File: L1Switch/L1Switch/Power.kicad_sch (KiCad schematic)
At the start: 60 parts, among them J3 Barrel_Jack, U3 TPS548A20RVE, U4 TPS565208, U5 TPS565208, U6 TPS565208

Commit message: Add some part info. Fix footprint size for 2kV caps. Add a plane cutout around the magnetics.
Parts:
- added M1, M2: Fan, Connector:FanPinHeader_1x03_P2.54mm_Vertical, symbol Motor:Fan_3pin
- C29, C30, C31: value 22 uF, 3.637 mΩ -> 22 uF, 3.637 mOhm; MFR Part# (none) -> GRM31CR61A226ME19L; Manufacturer (none) -> MuRata
- C32: value 2.2 nF, 1.268 Ω -> 2.2 nF, 1.268 Ohm; MFR Part# (none) -> CGA1A2X7R1E222K030BA; Manufacturer (none) -> TDK
- C33, C34: value 2.2 uF, 9.497 mΩ -> 2.2 uF, 9.497 mOhm; MFR Part# (none) -> GRM219R61E225KA12D; Manufacturer (none) -> MuRata
- C35: MFR Part# (none) -> C0805C104M5RACTU; Manufacturer (none) -> Kemet
- C36: value 470 pF, 5.548 Ω -> 470 pF, 5.548 Ohm; MFR Part# (none) -> CGA1A2X7R1H471K030BA; Manufacturer (none) -> TDK
- C37, C38, C39, C40, C41, C42: value 100 uF, 4.885 mΩ -> 100 uF, 4.885 mOhm; MFR Part# (none) -> GRM31CR60J107ME39L; Manufacturer (none) -> MuRata
- C43, C44, C50, C51, C57, C58: value 10 uF, 4.512 mΩ -> 10 uF, 4.512 mOhm; MFR Part# (none) -> GRM31CR61E106KA12L; Manufacturer (none) -> MuRata
- C45, C52, C59: value 100 nF, 1 mΩ -> 100 nF, 1 mOhm; MFR Part# (none) -> GRM155R71C104KA88D; Manufacturer (none) -> MuRata
- C46, C53, C60: MFR Part# (none) -> C0603C104Z3VACTU; Manufacturer (none) -> Kemet
- C47, C48, C49, C54, C55, C56, C61, C62, C63: value 22 uF, 1 mΩ -> 22 uF, 1 mOhm; MFR Part# (none) -> GRM188R60J226MEA0D; Manufacturer (none) -> MuRata
- D1: MFR Part# (none) -> P4SMA6.8CA; Manufacturer (none) -> Bourns
- F1: MFR Part# (none) -> 2920L700/12MR-A; Manufacturer (none) -> Littelfuse
- J3: MFR Part# (none) -> MJ-179PH; Manufacturer (none) -> Multicomp
- L1: value 1 uH, 3.5 mΩ -> 1 uH, 3.5 mOhm; MFR Part# (none) -> SRP1040-1R0M; Manufacturer (none) -> Bourns
- L2, L3, L4: value 2.2 uH, 13.2 mΩ -> 2.2 uH, 13.2 mOhm; MFR Part# (none) -> XAL5030-222MEB; Manufacturer (none) -> Coilcraft
- U3: MFR Part# (none) -> TPS548A20RVER; Manufacturer (none) -> Texas Instruments
- U4, U5, U6: MFR Part# (none) -> TPS565208DDCR; Manufacturer (none) -> Texas Instruments
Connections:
- net GND: now also M1.3 (-), M2.3 (-)
- net VIN_5V: now also M1.2 (+), M2.2 (+)
- no-connect marks 1 -> 3

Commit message: Update part numbers.
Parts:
- C32: MFR Part# CGA1A2X7R1E222K030BA -> CGA2B2X7R1H222K050BA
- C36: MFR Part# CGA1A2X7R1H471K030BA -> CGA2B2X7R1H471K050BA
- M1, M2: MFR Part# (none) -> 644874-3; Manufacturer (none) -> TE Connectivity
- R22: MFR Part# (none) -> RC0402FR-07249KL; Manufacturer (none) -> Yageo
- R23: MFR Part# (none) -> CRCW040244K2FKED; Manufacturer (none) -> Vishay
- R24: MFR Part# (none) -> RC0402FR-07105KL; Manufacturer (none) -> Yageo
- R25: MFR Part# (none) -> CRCW0402150KFKED; Manufacturer (none) -> Vishay
- R26: MFR Part# (none) -> RC0402FR-0768K1L; Manufacturer (none) -> Yageo
- R27: MFR Part# (none) -> CRCW04023R01FKED; Manufacturer (none) -> Vishay
- R28, R29, R31, R33, R35: value 10K -> 10K0; MFR Part# (none) -> CRCW040210K0FKED; Manufacturer (none) -> Vishay
- R30: MFR Part# (none) -> CRCW040233K2FKED; Manufacturer (none) -> Vishay
- R32: MFR Part# (none) -> CRCW040213K7FKED; Manufacturer (none) -> Vishay
- R34: MFR Part# (none) -> CRCW04023K09FKED; Manufacturer (none) -> Vishay
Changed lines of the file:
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@@
 (kicad_sch (version 20200608) (host eeschema "5.99.0-unknown-1973153~101~ubuntu20.04.1")
-  (page 12 12)
+  (page 1 12)
   (paper "B")
   (junction (at 26.67 80.01))
@@
   (junction (at 396.24 143.51))
   (junction (at 396.24 182.88))
-  (no_connect (at 340.36 93.98))
   (no_connect (at 345.44 55.88))
   (no_connect (at 356.87 93.98))
+  (no_connect (at 340.36 93.98))
   (wire (pts (xy 20.32 48.26) (xy 29.21 48.26))
     (stroke (width 0) (type solid) (color 0 0 0 0))
@@
       (effects (font (size 1.27 1.27)) hide)
     )
+    (property "MFR Part#" "RC0402FR-07249KL" (id 4) (at 88.9 92.71 0)
+      (effects (font (size 1.27 1.27)) hide)
+    )
+    (property "Manufacturer" "Yageo" (id 5) (at 88.9 92.71 0)
+      (effects (font (size 1.27 1.27)) hide)
+    )
   )
   (symbol (lib_id "Device:R_US") (at 88.9 102.87 0) (unit 1)
@@
       (effects (font (size 1.27 1.27)) hide)
     )
+    (property "MFR Part#" "CRCW040244K2FKED" (id 4) (at 88.9 102.87 0)
+      (effects (font (size 1.27 1.27)) hide)
+    )
+    (property "Manufacturer" "Vishay" (id 5) (at 88.9 102.87 0)
+      (effects (font (size 1.27 1.27)) hide)
+    )
   )
   (symbol (lib_id "Device:R_US") (at 92.71 81.28 90) (unit 1)
@@
       (effects (font (size 1.27 1.27)) hide)
     )
+    (property "MFR Part#" "RC0402FR-07105KL" (id 4) (at 92.71 81.28 0)
+      (effects (font (size 1.27 1.27)) hide)
+    )
+    (property "Manufacturer" "Yageo" (id 5) (at 92.71 81.28 0)
+      (effects (font (size 1.27 1.27)) hide)
+    )
   )
   (symbol (lib_id "Device:R_US") (at 99.06 77.47 0) (unit 1)
@@
       (effects (font (size 1.27 1.27)) hide)
     )
+    (property "MFR Part#" "CRCW0402150KFKED" (id 4) (at 99.06 77.47 0)
+      (effects (font (size 1.27 1.27)) hide)
+    )
+    (property "Manufacturer" "Vishay" (id 5) (at 99.06 77.47 0)
+      (effects (font (size 1.27 1.27)) hide)
+    )
   )
   (symbol (lib_id "Device:R_US") (at 162.56 156.21 0) (unit 1)
@@
       (effects (font (size 1.27 1.27)) hide)
     )
+    (property "MFR Part#" "CRCW040213K7FKED" (id 4) (at 162.56 156.21 0)
+      (effects (font (size 1.27 1.27)) hide)
+    )
+    (property "Manufacturer" "Vishay" (id 5) (at 162.56 156.21 0)
+      (effects (font (size 1.27 1.27)) hide)
+    )
   )
   (symbol (lib_id "Device:R_US") (at 162.56 175.26 0) (unit 1)
@@
       (effects (font (size 1.27 1.27)) (justify left))
     )
-    (property "Value" "10K" (id 1) (at 164.211 176.403 0)
+    (property "Value" "10K0" (id 1) (at 164.211 176.403 0)
       (effects (font (size 1.27 1.27)) (justify left))
     )
@@
       (effects (font (size 1.27 1.27)) hide)
     )
+    (property "MFR Part#" "CRCW040210K0FKED" (id 4) (at 162.56 175.26 0)
+      (effects (font (size 1.27 1.27)) hide)
+    )
+    (property "Manufacturer" "Vishay" (id 5) (at 162.56 175.26 0)
+      (effects (font (size 1.27 1.27)) hide)
+    )
   )
   (symbol (lib_id "Device:R_US") (at 162.56 226.06 0) (unit 1)
@@
       (effects (font (size 1.27 1.27)) hide)
     )
+    (property "MFR Part#" "CRCW040233K2FKED" (id 4) (at 162.56 226.06 0)
+      (effects (font (size 1.27 1.27)) hide)
+    )
+    (property "Manufacturer" "Vishay" (id 5) (at 162.56 226.06 0)
+      (effects (font (size 1.27 1.27)) hide)
+    )
   )
   (symbol (lib_id "Device:R_US") (at 162.56 245.11 0) (unit 1)
@@
       (effects (font (size 1.27 1.27)) (justify left))
     )
-    (property "Value" "10K" (id 1) (at 164.211 246.253 0)
+    (property "Value" "10K0" (id 1) (at 164.211 246.253 0)
       (effects (font (size 1.27 1.27)) (justify left))
     )
@@
       (effects (font (size 1.27 1.27)) hide)
     )
+    (property "MFR Part#" "CRCW040210K0FKED" (id 4) (at 162.56 245.11 0)
+      (effects (font (size 1.27 1.27)) hide)
+    )
+    (property "Manufacturer" "Vishay" (id 5) (at 162.56 245.11 0)
+      (effects (font (size 1.27 1.27)) hide)
+    )
   )
   (symbol (lib_id "Device:R_US") (at 167.64 85.09 0) (unit 1)
@@
       (effects (font (size 1.27 1.27)) hide)
     )
+    (property "MFR Part#" "RC0402FR-0768K1L" (id 4) (at 167.64 85.09 0)
+      (effects (font (size 1.27 1.27)) hide)
+    )
+    (property "Manufacturer" "Yageo" (id 5) (at 167.64 85.09 0)
+      (effects (font (size 1.27 1.27)) hide)
+    )
   )
   (symbol (lib_id "Device:R_US") (at 181.61 91.44 0) (unit 1)
@@
       (effects (font (size 1.27 1.27)) hide)
     )
+    (property "MFR Part#" "CRCW04023R01FKED" (id 4) (at 181.61 91.44 0)
+      (effects (font (size 1.27 1.27)) hide)
+    )
+    (property "Manufacturer" "Vishay" (id 5) (at 181.61 91.44 0)
+      (effects (font (size 1.27 1.27)) hide)
+    )
   )
   (symbol (lib_id "Device:R_US") (at 212.09 59.69 0) (unit 1)
@@
       (effects (font (size 1.27 1.27)) (justify left))
     )
-    (property "Value" "10K" (id 1) (at 213.741 60.833 0)
+    (property "Value" "10K0" (id 1) (at 213.741 60.833 0)
       (effects (font (size 1.27 1.27)) (justify left))
     )
@@
       (effects (font (size 1.27 1.27)) hide)
     )
+    (property "MFR Part#" "CRCW040210K0FKED" (id 4) (at 212.09 59.69 0)
+      (effects (font (size 1.27 1.27)) hide)
+    )
+    (property "Manufacturer" "Vishay" (id 5) (at 212.09 59.69 0)
+      (effects (font (size 1.27 1.27)) hide)
+    )
   )
   (symbol (lib_id "Device:R_US") (at 212.09 78.74 0) (unit 1)
@@
       (effects (font (size 1.27 1.27)) (justify left))
     )
-    (property "Value" "10K" (id 1) (at 213.741 79.883 0)
+    (property "Value" "10K0" (id 1) (at 213.741 79.883 0)
       (effects (font (size 1.27 1.27)) (justify left))
     )
@@
       (effects (font (size 1.27 1.27)) hide)
     )
+    (property "MFR Part#" "CRCW040210K0FKED" (id 4) (at 212.09 78.74 0)
+      (effects (font (size 1.27 1.27)) hide)
+    )
+    (property "Manufacturer" "Vishay" (id 5) (at 212.09 78.74 0)
+      (effects (font (size 1.27 1.27)) hide)
+    )
   )
   (symbol (lib_id "Device:R_US") (at 356.87 156.21 0) (unit 1)
@@
       (effects (font (size 1.27 1.27)) hide)
     )
+    (property "MFR Part#" "CRCW04023K09FKED" (id 4) (at 356.87 156.21 0)
+      (effects (font (size 1.27 1.27)) hide)
+    )
+    (property "Manufacturer" "Vishay" (id 5) (at 356.87 156.21 0)
+      (effects (font (size 1.27 1.27)) hide)
+    )
   )
   (symbol (lib_id "Device:R_US") (at 356.87 175.26 0) (unit 1)
@@
       (effects (font (size 1.27 1.27)) (justify left))
     )
-    (property "Value" "10K" (id 1) (at 358.521 176.403 0)
+    (property "Value" "10K0" (id 1) (at 358.521 176.403 0)
       (effects (font (size 1.27 1.27)) (justify left))
     )
@@
     )
     (property "Datasheet" "~" (id 3) (at 356.87 175.26 0)
+      (effects (font (size 1.27 1.27)) hide)
+    )
+    (property "MFR Part#" "CRCW040210K0FKED" (id 4) (at 356.87 175.26 0)
+      (effects (font (size 1.27 1.27)) hide)
+    )
+    (property "Manufacturer" "Vishay" (id 5) (at 356.87 175.26 0)
       (effects (font (size 1.27 1.27)) hide)
     )
@@
       (effects (font (size 1.27 1.27)) hide)
     )
-    (property "MFR Part#" "CGA1A2X7R1E222K030BA" (id 4) (at 69.85 63.5 0)
+    (property "MFR Part#" "CGA2B2X7R1H222K050BA" (id 4) (at 69.85 63.5 0)
       (effects (font (size 1.27 1.27)) hide)
     )
@@
       (effects (font (size 1.27 1.27)) hide)
     )
-    (property "MFR Part#" "CGA1A2X7R1H471K030BA" (id 4) (at 181.61 74.93 0)
+    (property "MFR Part#" "CGA2B2X7R1H471K050BA" (id 4) (at 181.61 74.93 0)
       (effects (font (size 1.27 1.27)) hide)
     )
@@
       (effects (font (size 1.27 1.27)) hide)
     )
+    (property "MFR Part#" "644874-3" (id 4) (at 347.98 93.98 0)
+      (effects (font (size 1.27 1.27)) hide)
+    )
+    (property "Manufacturer" "TE Connectivity" (id 5) (at 347.98 93.98 0)
+      (effects (font (size 1.27 1.27)) hide)
+    )
   )
   (symbol (lib_id "Motor:Fan_3pin") (at 364.49 93.98 0) (unit 1)
@@
       (effects (font (size 1.27 1.27)) hide)
     )
+    (property "MFR Part#" "644874-3" (id 4) (at 364.49 93.98 0)
+      (effects (font (size 1.27 1.27)) hide)
+    )
+    (property "Manufacturer" "TE Connectivity" (id 5) (at 364.49 93.98 0)
+      (effects (font (size 1.27 1.27)) hide)
+    )

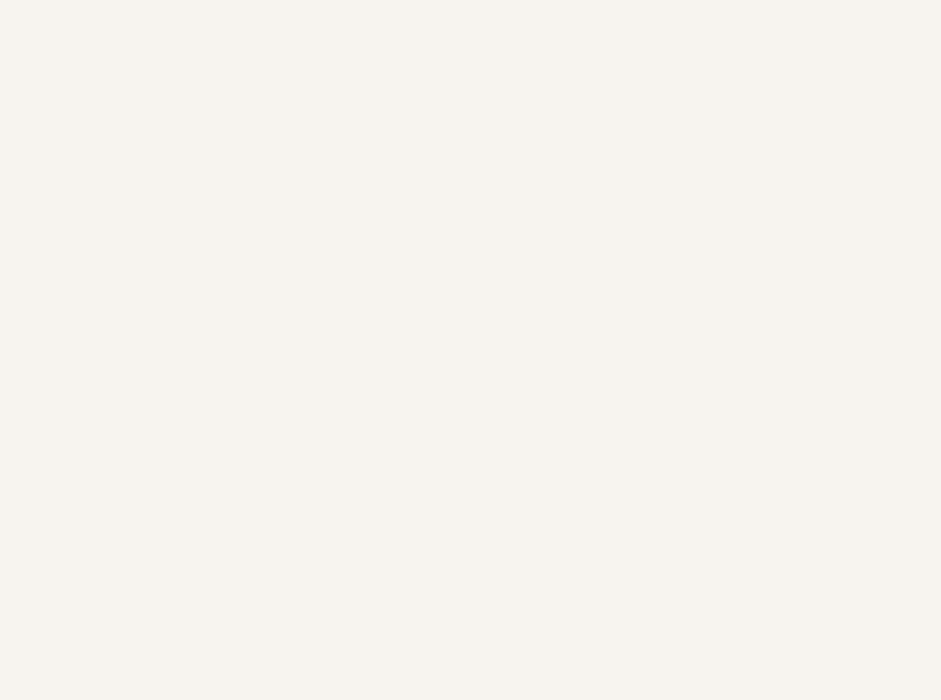
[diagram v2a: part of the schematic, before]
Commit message: Finish length matching. Move the layout onto a larger sheet to fit.
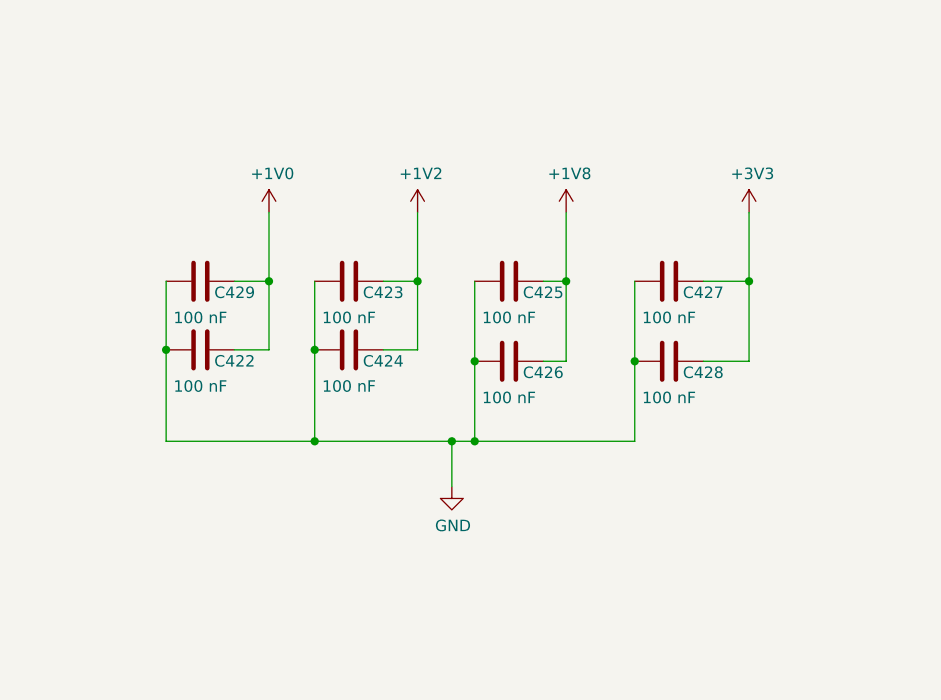
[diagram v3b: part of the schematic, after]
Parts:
- added C422, C423, C424, C425, C426, C427, C428, C429: 100 nF, Capacitor_SMD:C_0402_1005Metric, symbol Device:C
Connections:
- net +1V0: now also C422.1, C429.1
- net +1V2: now also C423.1, C424.1
- net +1V8: now also C425.1, C426.1
- net +3V3: now also C427.1, C428.1
- net GND: now also C422.2, C423.2, C424.2, C425.2, C426.2, C427.2, C428.2, C429.2

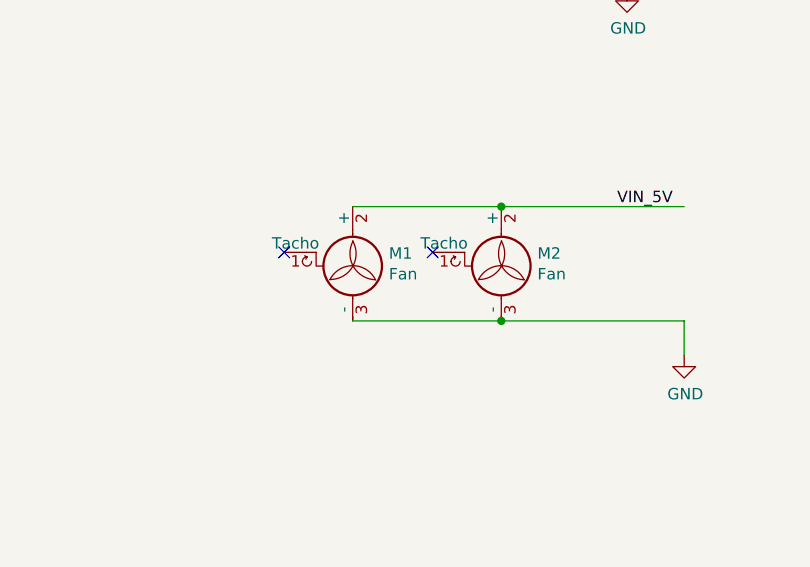
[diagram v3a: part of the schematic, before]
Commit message: Swap fan connector orientation. Add PU/PD for JTAG pins.
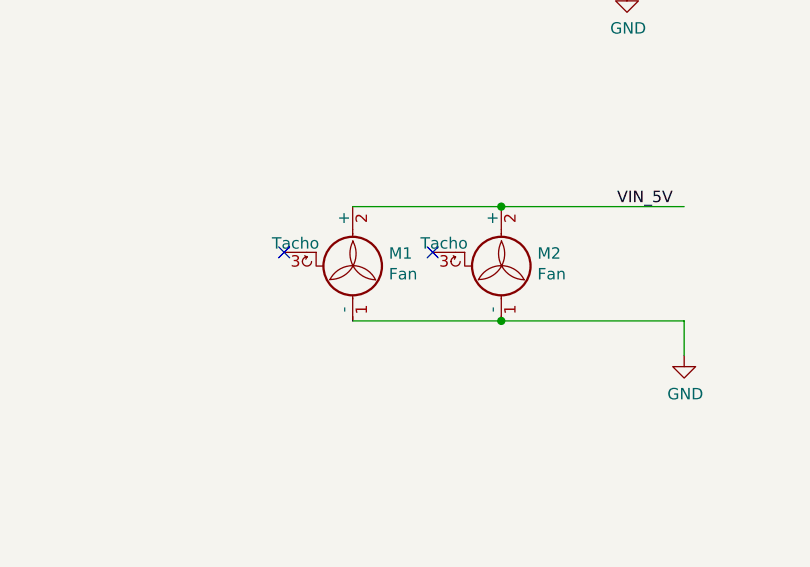
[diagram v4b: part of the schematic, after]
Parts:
- M1, M2: symbol Motor:Fan_3pin -> L1Switch:Fan_Tacho
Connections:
- net GND: now also M1.1 (-), M2.1 (-); no longer M1.3 (-), M2.3 (-)
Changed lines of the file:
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@@
   (junction (at 396.24 143.51))
   (junction (at 396.24 182.88))
+  (no_connect (at 340.36 93.98))
   (no_connect (at 345.44 55.88))
-  (no_connect (at 340.36 93.98))
   (no_connect (at 356.87 93.98))
   (wire (pts (xy 20.32 48.26) (xy 29.21 48.26))
@@
     )
   )
-  (symbol (lib_id "Motor:Fan_3pin") (at 347.98 93.98 0) (unit 1)
+  (symbol (lib_id "L1Switch:Fan_Tacho") (at 347.98 93.98 0) (unit 1)
     (in_bom yes) (on_board yes)
     (property "Reference" "M1" (id 0) (at 351.9933 94.1006 0)
@@
     )
   )
-  (symbol (lib_id "Motor:Fan_3pin") (at 364.49 93.98 0) (unit 1)
+  (symbol (lib_id "L1Switch:Fan_Tacho") (at 364.49 93.98 0) (unit 1)
     (in_bom yes) (on_board yes)
     (property "Reference" "M2" (id 0) (at 368.5033 94.1006 0)
